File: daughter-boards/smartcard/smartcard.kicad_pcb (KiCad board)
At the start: 2 copper layers, 41 x 92 mm, 46 parts, among them P1 SAMTEC-QSE-020-01-F-D-A, P2 SAMTEC-QSE-020-01-F-D-A, U1 7334L2622F04LF

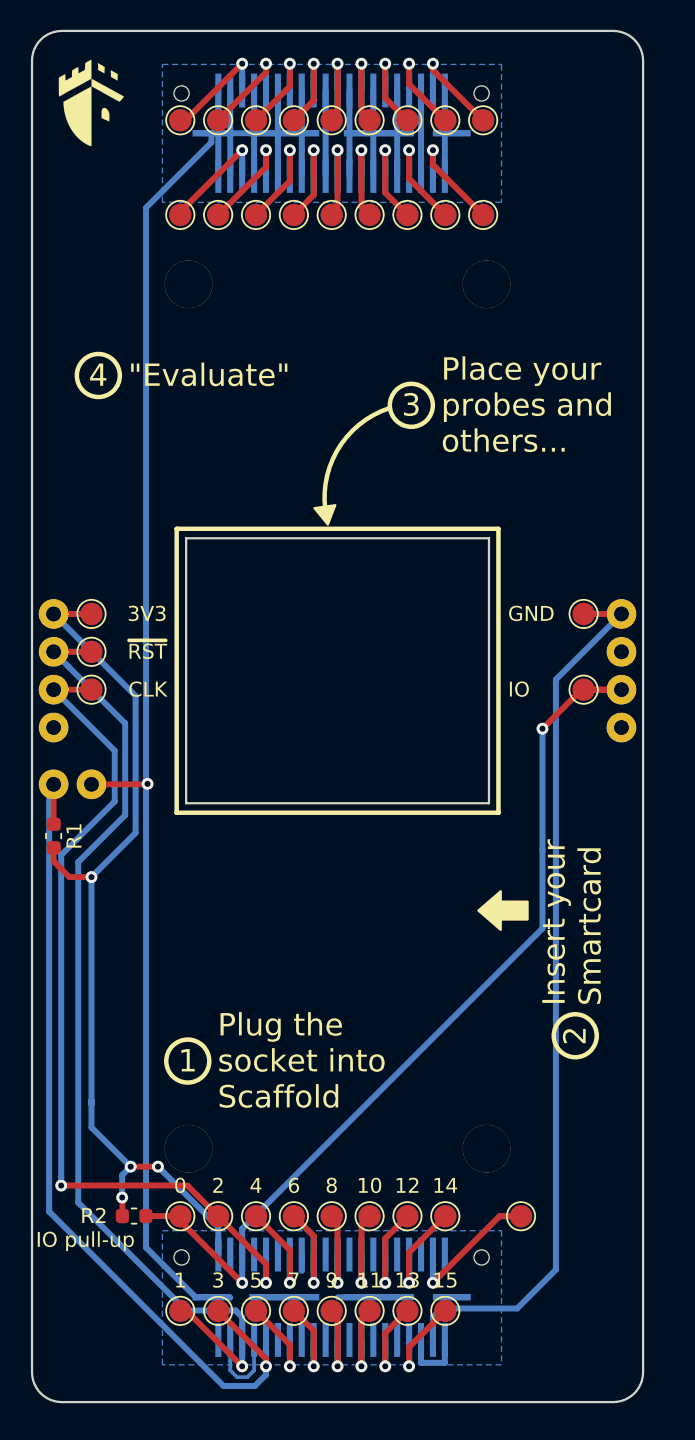
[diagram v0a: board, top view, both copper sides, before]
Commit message: Updated daughterboards for the new Scaffold socket
Update breadboard, smartcard and STM32F205 daughterboards to fit the
new socket format of Scaffold v1.1 hardware.
Previous socket format is now deprecated.
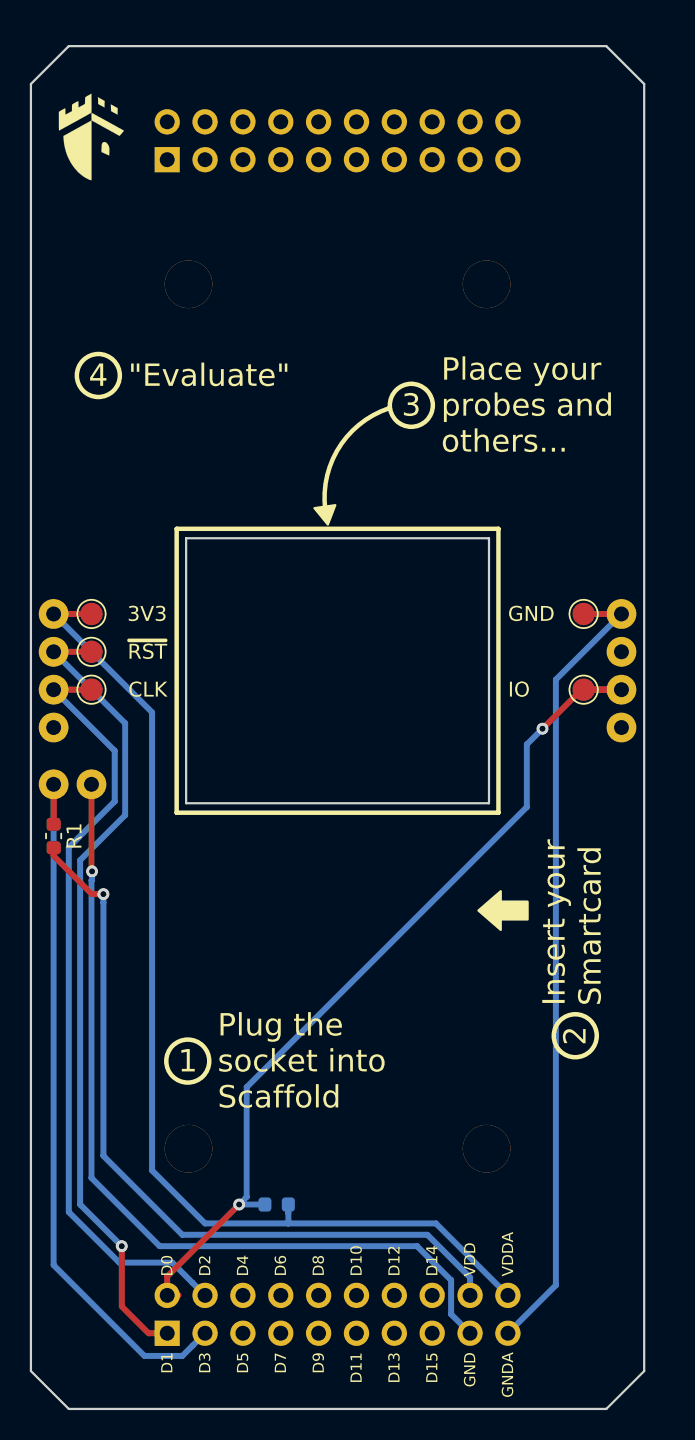
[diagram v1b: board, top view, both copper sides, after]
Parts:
- removed P1, P2: SAMTEC-QSE-020-01-F-D-A, mykicadlibs:SAMTEC-QSE-020-01-F-D-A
- removed TP1, TP10, TP11, TP12, TP13, TP14, TP15, TP16, TP17, TP2, TP3, TP34, TP35, TP36, TP37, TP38, TP39, TP4, TP40, TP41, TP42, TP43, TP44, TP45, TP46, TP47, TP48, TP49, TP5, TP50, TP51, TP6, TP7, TP8, TP9: TestPoint, TestPoint:TestPoint_Pad_D1.5mm
- added J1: Conn_02x10_Odd_Even, Connector_PinSocket_2.54mm:PinSocket_2x10_P2.54mm_Vertical, B.Cu at (100.7, 145.4)
- added J2: Conn_02x10_Odd_Even, Connector_PinSocket_2.54mm:PinSocket_2x10_P2.54mm_Vertical, B.Cu at (100.7, 66.7)
- R2: moved to B.Cu
- moved R2 9.59 mm to (108.1, 136.8), turned to 0 degrees
- moved LOGO1 2.29 mm to (95.6, 65.1)
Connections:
- R1 pad 1: +3V3 -> VDD
- R2 pad 2: +3V3 -> VDDA
- TP33 pad 1: +3V3 -> VDDA
- U1 pad 1: +3V3 -> VDDA
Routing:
- net GND: track 171.3 -> 57.5 mm
- net VDDA: track 0.00 -> 71.2 mm
- net +3V3: track 62.3 -> 0.00 mm, vias 4 -> 0
- net VDD: track 0.00 -> 51.7 mm, vias 0 -> 1
- net /D3_SENSE: track 60.8 -> 48.7 mm, vias 1 -> 0
- net /D1_~RST~: track 66.0 -> 54.7 mm
- net Net-(P1-Pad4): track 9.66 -> 0.00 mm, vias 1 -> 0
- net Net-(P2-Pad35): track 7.80 -> 0.00 mm, vias 1 -> 0
- net Net-(P2-Pad36): track 7.52 -> 0.00 mm, vias 1 -> 0
- net Net-(P2-Pad3): track 7.47 -> 0.00 mm, vias 1 -> 0
- net Net-(P2-Pad31): track 7.41 -> 0.00 mm, vias 1 -> 0
- net Net-(P1-Pad8): track 7.38 -> 0.00 mm, vias 1 -> 0
- net Net-(P1-Pad28): track 7.31 -> 0.00 mm, vias 1 -> 0
- net Net-(P2-Pad7): track 7.08 -> 0.00 mm, vias 1 -> 0
- net Net-(P2-Pad27): track 7.02 -> 0.00 mm, vias 1 -> 0
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- removed copper zone on B.Cu, net GND
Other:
- board size 41 x 92 mm -> 41.1 x 91.4 mm
- board text added: "D0"
- board text added: "D1"
- board text added: "D10"
- board text added: "D11"
- board text added: "D12"
- board text added: "D13"
- board text added: "D14"
- board text added: "D15"
- board text added: "D2"
- board text added: "D3"
- board text added: "D4"
- board text added: "D5"
- board text added: "D6"
- board text added: "D7"
- board text added: "D8"
- board text added: "D9"
- board text added: "GNDA"
- board text added: "VDD"
- board text added: "VDDA"
- board text removed: "0"
- board text removed: "10"
- board text removed: "11"
- board text removed: "12"
- board text removed: "13"
- board text removed: "14"
- board text removed: "15"
- board text removed: "6"
- board text removed: "7"
- board text removed: "8"
- board text removed: "9"
